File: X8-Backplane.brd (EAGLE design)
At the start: 101.6 x 101.6 mm, 4 parts

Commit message: Fleshing out the idea for the backplane
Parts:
- moved U$18 94.3 mm to (26.2, 82.3), turned to 270 degrees
- moved U$2 31.6 mm to (54.4, 31.8)
- moved U$1 22.7 mm to (89.2, 39.6)
- moved U$17 9.80 mm to (69.6, 39.9)
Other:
- outline, holes or cut-outs redrawn
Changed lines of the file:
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@@
 <setting verticaltext="up"/>
 </settings>
-<grid distance="0.05" unitdist="inch" unit="inch" style="lines" multiple="1" display="no" altdistance="0.025" altunitdist="inch" altunit="inch"/>
+<grid distance="0.01" unitdist="inch" unit="inch" style="lines" multiple="1" display="no" altdistance="0.025" altunitdist="inch" altunit="inch"/>
 <layers>
 <layer number="1" name="Top" color="4" fill="1" visible="yes" active="yes"/>
@@
 <layer number="42" name="bRestrict" color="1" fill="10" visible="no" active="yes"/>
 <layer number="43" name="vRestrict" color="2" fill="10" visible="no" active="yes"/>
-<layer number="44" name="Drills" color="7" fill="1" visible="yes" active="yes"/>
+<layer number="44" name="Drills" color="7" fill="1" visible="no" active="yes"/>
 <layer number="45" name="Holes" color="7" fill="1" visible="yes" active="yes"/>
-<layer number="46" name="Milling" color="3" fill="1" visible="yes" active="yes"/>
-<layer number="47" name="Measures" color="7" fill="1" visible="yes" active="yes"/>
-<layer number="48" name="Document" color="7" fill="1" visible="yes" active="yes"/>
+<layer number="46" name="Milling" color="3" fill="1" visible="no" active="yes"/>
+<layer number="47" name="Measures" color="7" fill="1" visible="no" active="yes"/>
+<layer number="48" name="Document" color="7" fill="1" visible="no" active="yes"/>
 <layer number="49" name="Reference" color="7" fill="1" visible="no" active="yes"/>
 <layer number="50" name="dxf" color="7" fill="1" visible="no" active="no"/>
-<layer number="51" name="tDocu" color="7" fill="1" visible="no" active="yes"/>
-<layer number="52" name="bDocu" color="7" fill="1" visible="no" active="yes"/>
+<layer number="51" name="tDocu" color="7" fill="1" visible="yes" active="yes"/>
+<layer number="52" name="bDocu" color="7" fill="1" visible="yes" active="yes"/>
 <layer number="53" name="tGND_GNDA" color="7" fill="1" visible="no" active="no"/>
 <layer number="54" name="bGND_GNDA" color="7" fill="1" visible="no" active="no"/>
@@
 <wire x1="100" y1="0" x2="100" y2="80" width="0" layer="20"/>
 <wire x1="100" y1="80" x2="0" y2="80" width="0" layer="20"/>
-<wire x1="0" y1="80" x2="0" y2="0" width="0" layer="20"/>
-<circle x="50.8" y="38.1" radius="50.8" width="0.4064" layer="20"/>
+<wire x1="0" y1="80" x2="0" y2="59.69" width="0" layer="20"/>
+<wire x1="0" y1="17.78" x2="0" y2="0" width="0" layer="20"/>
+<wire x1="0" y1="59.69" x2="0" y2="17.78" width="0.4064" layer="20"/>
+<wire x1="29.21" y1="-12.7" x2="72.39" y2="-12.7" width="0.4064" layer="20"/>
+<wire x1="101.6" y1="17.78" x2="101.6" y2="59.69" width="0.4064" layer="20"/>
+<wire x1="72.39" y1="88.9" x2="29.21" y2="88.9" width="0.4064" layer="20"/>
+<wire x1="0" y1="59.69" x2="14.732" y2="74.422" width="0.4064" layer="20"/>
+<wire x1="14.732" y1="74.422" x2="29.21" y2="88.9" width="0.4064" layer="20"/>
+<wire x1="29.21" y1="-12.7" x2="0" y2="17.78" width="0.4064" layer="20"/>
+<wire x1="101.6" y1="59.69" x2="72.39" y2="88.9" width="0.4064" layer="20"/>
+<wire x1="101.6" y1="17.78" x2="72.39" y2="-12.7" width="0.4064" layer="20"/>
+<hole x="21.59" y="67.818" drill="3.2"/>
+<hole x="80.01" y="66.802" drill="3.2"/>
+<hole x="21.59" y="9.398" drill="3.2"/>
+<hole x="80.01" y="9.398" drill="3.2"/>
+<wire x1="14.986" y1="74.422" x2="14.732" y2="74.422" width="0.4064" layer="20"/>
 </plain>
 <attributes>
@@
 </autorouter>
 <elements>
-<element name="U$1" library="HSEC8-1xx-01-XX-DV-A" package="HSEC8-140-01-XX-DV-A" value="HSEC8-140-01-XX-DV-A" x="67.31" y="45.72" rot="R90"/>
-<element name="U$17" library="HSEC8-1xx-01-XX-DV-A" package="HSEC8-140-01-XX-DV-A" value="HSEC8-140-01-XX-DV-A" x="77.47" y="45.72" rot="R90"/>
-<element name="U$2" library="HSEC8-1xx-01-XX-DV-A" package="HSEC8-160-01-XX-DV-A" value="HSEC8-160-01-XX-DV-A" x="25.4" y="44.45" rot="R90"/>
-<element name="U$18" library="Other" package="ETH_SWITCH" value="" x="58.42" y="-6.35" rot="R90"/>
+<element name="U$1" library="HSEC8-1xx-01-XX-DV-A" package="HSEC8-140-01-XX-DV-A" value="HSEC8-140-01-XX-DV-A" x="89.154" y="39.624" rot="R90"/>
+<element name="U$17" library="HSEC8-1xx-01-XX-DV-A" package="HSEC8-140-01-XX-DV-A" value="HSEC8-140-01-XX-DV-A" x="69.596" y="39.878" rot="R90"/>
+<element name="U$18" library="Other" package="ETH_SWITCH" value="" x="26.162" y="82.296" rot="R270"/>
+<element name="U$2" library="HSEC8-1xx-01-XX-DV-A" package="HSEC8-160-01-XX-DV-A" value="HSEC8-160-01-XX-DV-A" x="54.356" y="31.75" rot="R90"/>
 </elements>
 <signals>

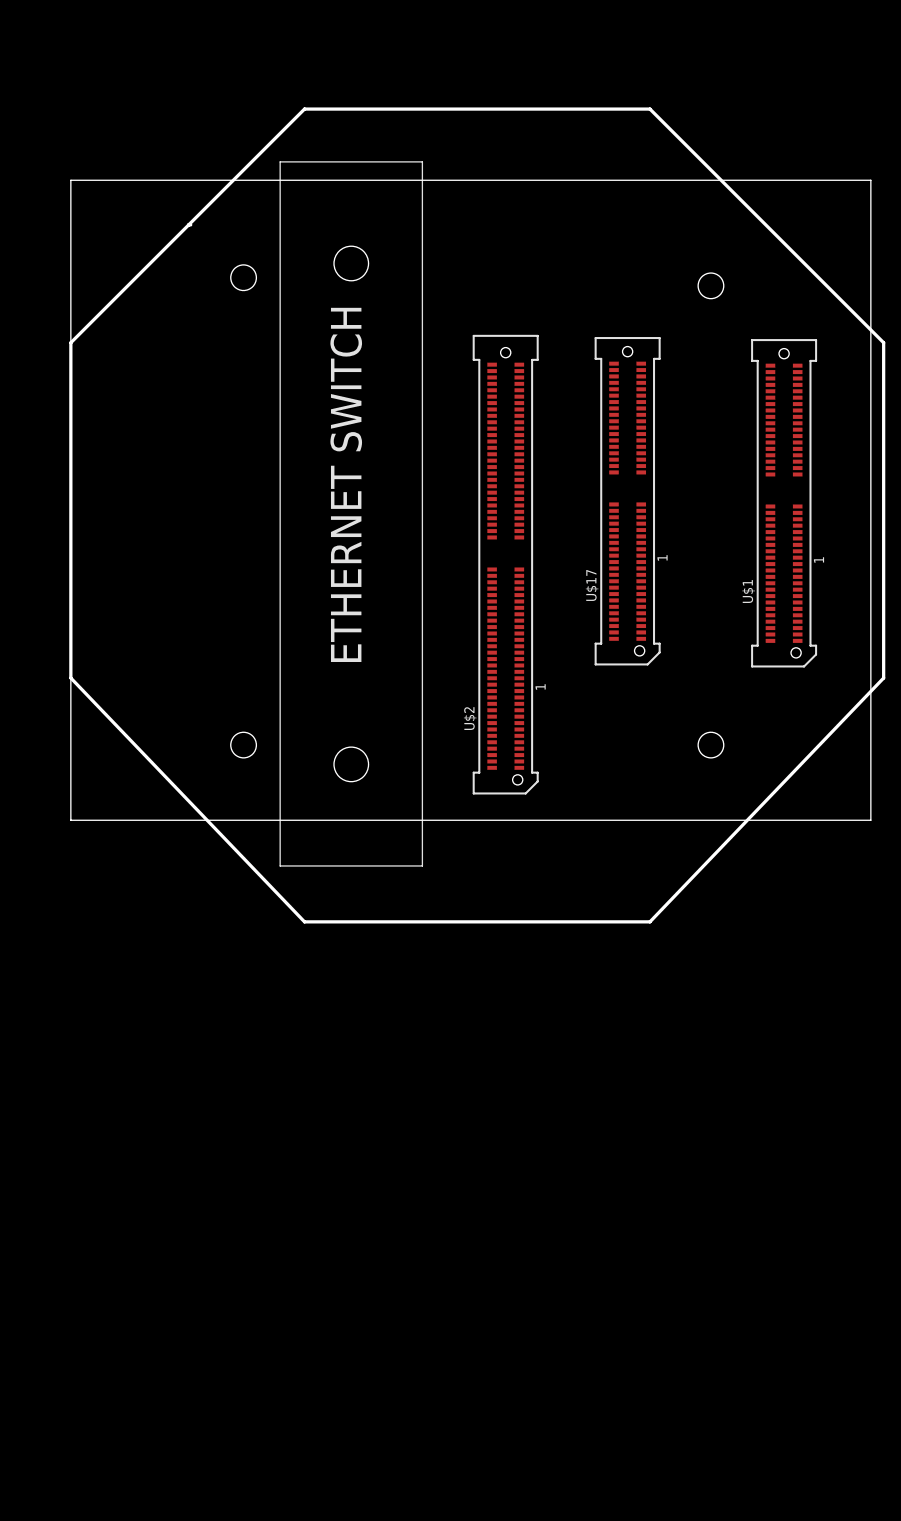
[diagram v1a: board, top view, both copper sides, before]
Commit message: Added more connections to the backplane
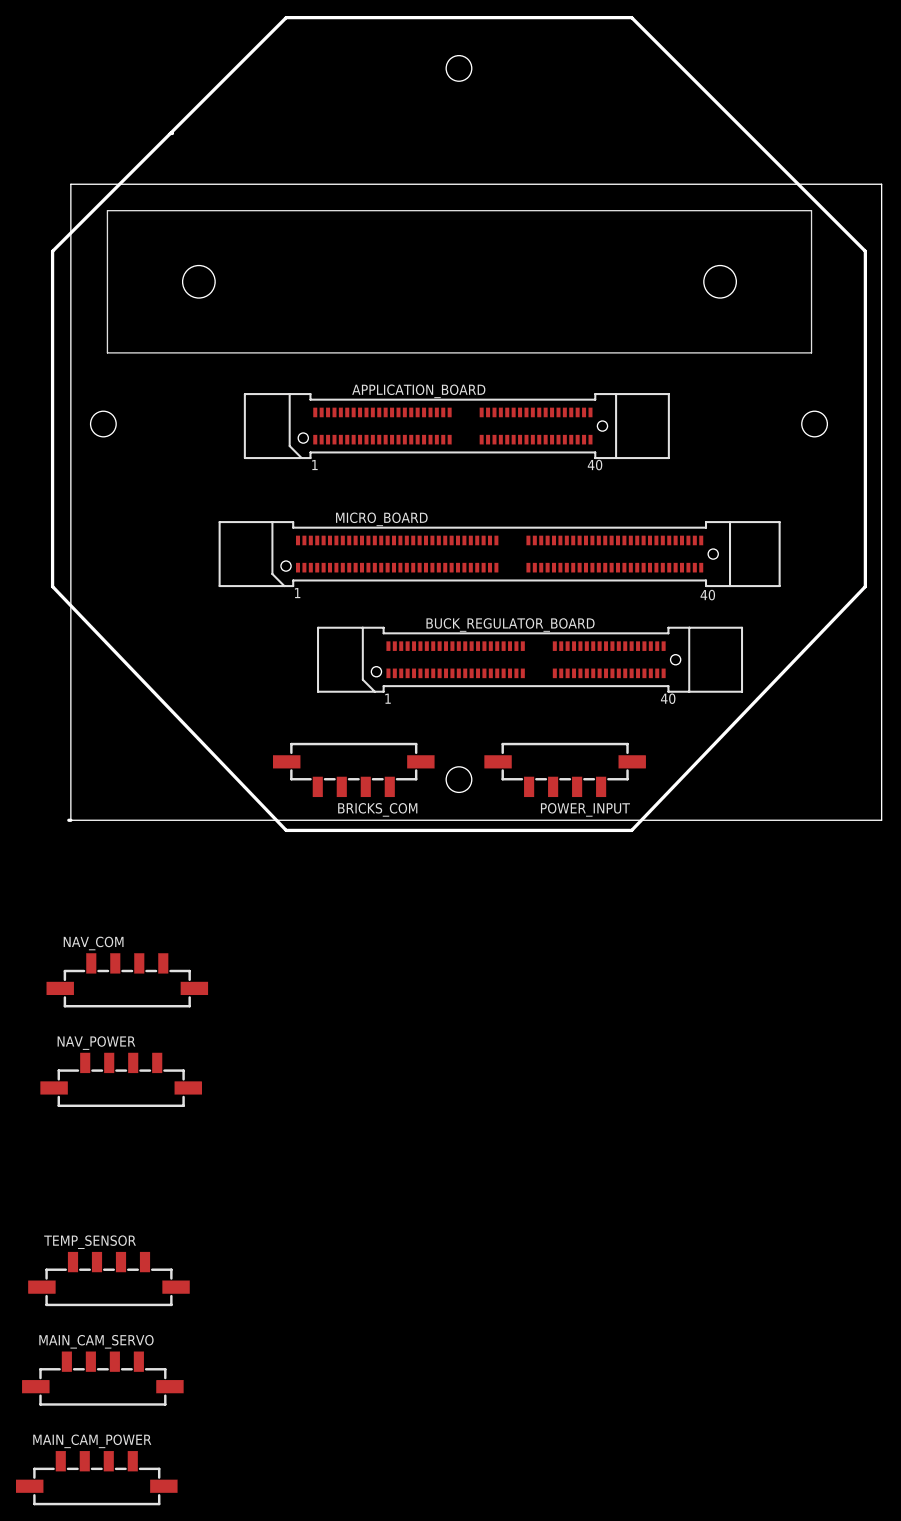
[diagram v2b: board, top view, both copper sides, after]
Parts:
- removed U$1, U$17: HSEC8-140-01-XX-DV-A, HSEC8-1xx-01-XX-DV-A:HSEC8-140-01-XX-DV-A
- removed U$2: HSEC8-160-01-XX-DV-A, HSEC8-1xx-01-XX-DV-A:HSEC8-160-01-XX-DV-A
- added APPLICATION_BOARD, BUCK_REGULATOR_BOARD: HSEC8-140-01-XX-DV-A, HSEC8-1xx-01-XX-DV-A:HSEC8-140-01-XX-DV-A
- added BRICKS_COM, MAIN_CAM_POWER, MAIN_CAM_SERVO, NAV_COM, NAV_POWER, POWER_INPUT, TEMP_SENSOR: MICRO-FIT-4-SMD-PART, Connectors:MICRO-FIT-4-SMD
- added MICRO_BOARD: HSEC8-160-01-XX-DV-A, HSEC8-1xx-01-XX-DV-A:HSEC8-160-01-XX-DV-A
- moved U$18 32.2 mm to (4.57, 58.4), turned to 0 degrees
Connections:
- new net +12V: BUCK_REGULATOR_BOARD.31, BUCK_REGULATOR_BOARD.32, BUCK_REGULATOR_BOARD.33, BUCK_REGULATOR_BOARD.34, BUCK_REGULATOR_BOARD.35, BUCK_REGULATOR_BOARD.36, BUCK_REGULATOR_BOARD.37, BUCK_REGULATOR_BOARD.38, BUCK_REGULATOR_BOARD.39, BUCK_REGULATOR_BOARD.40, BUCK_REGULATOR_BOARD.41, BUCK_REGULATOR_BOARD.42, BUCK_REGULATOR_BOARD.43, BUCK_REGULATOR_BOARD.44, BUCK_REGULATOR_BOARD.45, BUCK_REGULATOR_BOARD.46, BUCK_REGULATOR_BOARD.47, BUCK_REGULATOR_BOARD.48, BUCK_REGULATOR_BOARD.49, BUCK_REGULATOR_BOARD.50, BUCK_REGULATOR_BOARD.51, BUCK_REGULATOR_BOARD.52, MAIN_CAM_POWER.C4, NAV_POWER.C4, POWER_INPUT.C3, POWER_INPUT.C4
- new net +3V3: TEMP_SENSOR.C3
- new net +5V: BUCK_REGULATOR_BOARD.10, BUCK_REGULATOR_BOARD.11, BUCK_REGULATOR_BOARD.12, BUCK_REGULATOR_BOARD.13, BUCK_REGULATOR_BOARD.14, BUCK_REGULATOR_BOARD.15, BUCK_REGULATOR_BOARD.16, BUCK_REGULATOR_BOARD.17, BUCK_REGULATOR_BOARD.18, BUCK_REGULATOR_BOARD.19, BUCK_REGULATOR_BOARD.20, BUCK_REGULATOR_BOARD.21, BUCK_REGULATOR_BOARD.22, BUCK_REGULATOR_BOARD.23, BUCK_REGULATOR_BOARD.24, BUCK_REGULATOR_BOARD.25, BUCK_REGULATOR_BOARD.26, BUCK_REGULATOR_BOARD.5, BUCK_REGULATOR_BOARD.6, BUCK_REGULATOR_BOARD.7, BUCK_REGULATOR_BOARD.8, BUCK_REGULATOR_BOARD.9, MAIN_CAM_SERVO.C3, NAV_POWER.C3
- new net BUCK_SCL: BUCK_REGULATOR_BOARD.1, BUCK_REGULATOR_BOARD.2
- new net BUCK_SDA: BUCK_REGULATOR_BOARD.3, BUCK_REGULATOR_BOARD.4
- new net CANH: BRICKS_COM.C4
- new net CANL: BRICKS_COM.C3
- new net GND: BUCK_REGULATOR_BOARD.55, BUCK_REGULATOR_BOARD.56, BUCK_REGULATOR_BOARD.57, BUCK_REGULATOR_BOARD.58, BUCK_REGULATOR_BOARD.59, BUCK_REGULATOR_BOARD.60, BUCK_REGULATOR_BOARD.61, BUCK_REGULATOR_BOARD.62, BUCK_REGULATOR_BOARD.63, BUCK_REGULATOR_BOARD.64, BUCK_REGULATOR_BOARD.65, BUCK_REGULATOR_BOARD.66, BUCK_REGULATOR_BOARD.67, BUCK_REGULATOR_BOARD.68, BUCK_REGULATOR_BOARD.69, BUCK_REGULATOR_BOARD.70, BUCK_REGULATOR_BOARD.71, BUCK_REGULATOR_BOARD.72, BUCK_REGULATOR_BOARD.73, BUCK_REGULATOR_BOARD.74, BUCK_REGULATOR_BOARD.75, BUCK_REGULATOR_BOARD.76, BUCK_REGULATOR_BOARD.77, BUCK_REGULATOR_BOARD.78, BUCK_REGULATOR_BOARD.79, BUCK_REGULATOR_BOARD.80, MAIN_CAM_POWER.C1, MAIN_CAM_POWER.C2, MAIN_CAM_SERVO.C2, NAV_POWER.C1, NAV_POWER.C2, POWER_INPUT.C1, POWER_INPUT.C2, TEMP_SENSOR.C2
- new net LED_PWM: MAIN_CAM_POWER.C3
- new net MAIN_SERVO: MAIN_CAM_SERVO.C4
- new net N$3: BRICKS_COM.C2
- new net N$5: BRICKS_COM.C1
- new net N$7: TEMP_SENSOR.C1
- new net SCL: NAV_COM.C4
- new net SDA: NAV_COM.C3
- new net SONAR_DAC: NAV_COM.C1
- new net SONAR_PWM: NAV_COM.C2
- new net TEMP_DATA: TEMP_SENSOR.C4
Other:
- board size 101.6 x 101.6 mm -> 103.6 x 101.6 mm

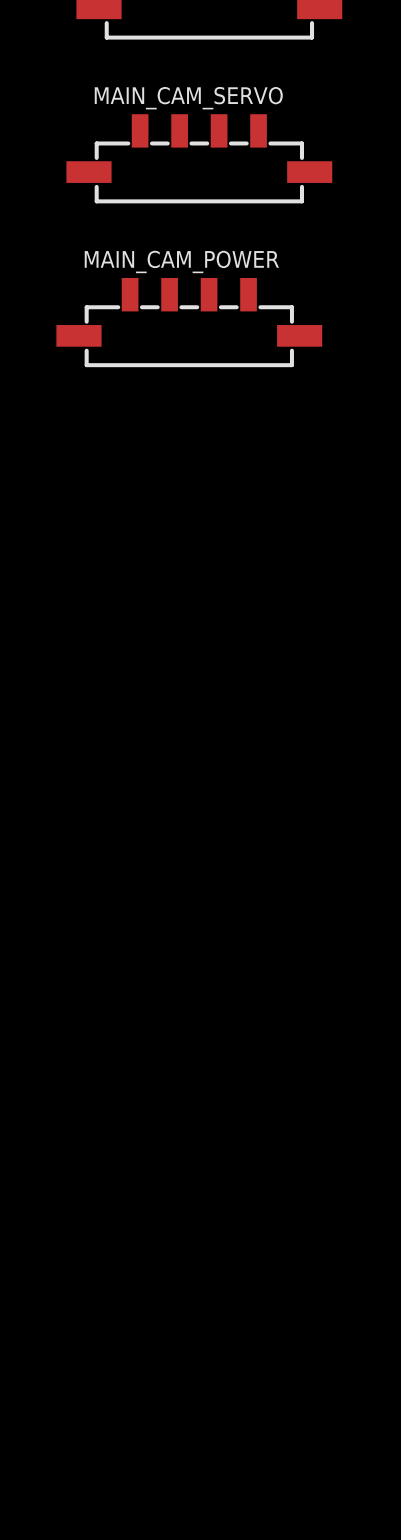
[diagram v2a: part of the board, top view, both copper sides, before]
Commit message: Added more connectors to the backplane schematic
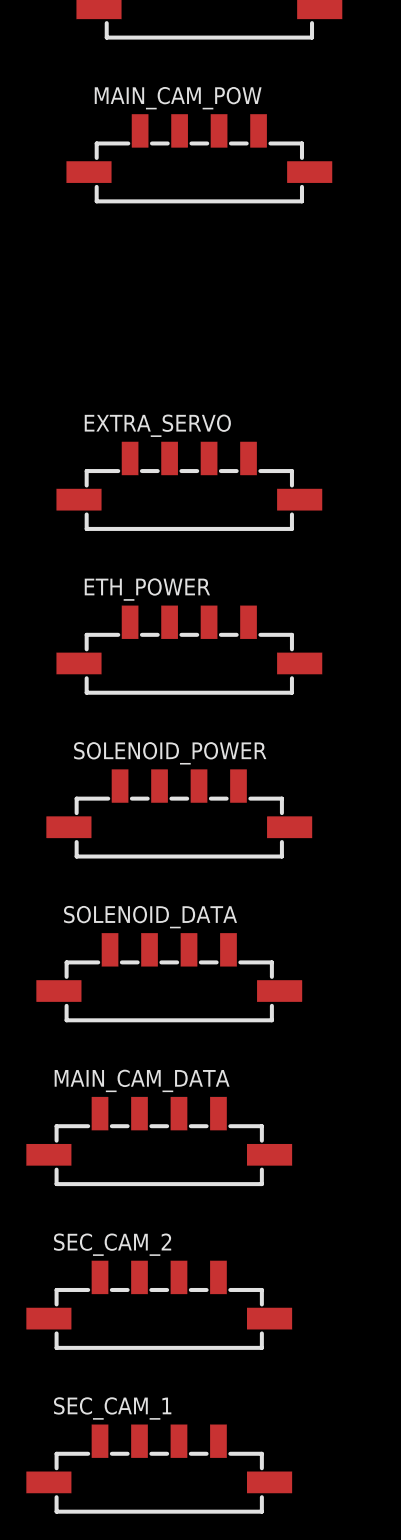
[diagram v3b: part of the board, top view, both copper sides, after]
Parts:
- removed MAIN_CAM_POWER: MICRO-FIT-4-SMD-PART, Connectors:MICRO-FIT-4-SMD
- added ETH_POWER, EXTRA_SERVO, MAIN_CAM_DATA, SEC_CAM_1, SEC_CAM_2, SOLENOID_DATA, SOLENOID_POWER: MICRO-FIT-4-SMD-PART, Connectors:MICRO-FIT-4-SMD
- renumbered MAIN_CAM_SERVO to MAIN_CAM_POW
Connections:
- new net CLK: SOLENOID_DATA.C3
- new net DATA: SOLENOID_DATA.C1
- new net ENABLE: SOLENOID_DATA.C2
- new net SECOND_SERVO: EXTRA_SERVO.C4
- net +12V: now also MAIN_CAM_POW.C4, SEC_CAM_1.C3, SEC_CAM_1.C4, SEC_CAM_2.C3, SEC_CAM_2.C4, SOLENOID_POWER.C3, SOLENOID_POWER.C4; no longer MAIN_CAM_POWER.C4
- net +5V: now also ETH_POWER.C3, ETH_POWER.C4, EXTRA_SERVO.C3, MAIN_CAM_POW.C2, SOLENOID_DATA.C4
- net GND: now also ETH_POWER.C1, ETH_POWER.C2, EXTRA_SERVO.C2, MAIN_CAM_DATA.C1, MAIN_CAM_DATA.C2, MAIN_CAM_POW.C1, SEC_CAM_1.C1, SEC_CAM_1.C2, SEC_CAM_2.C1, SEC_CAM_2.C2, SOLENOID_POWER.C1, SOLENOID_POWER.C2; no longer MAIN_CAM_POW.C2, MAIN_CAM_POWER.C1, MAIN_CAM_POWER.C2
- net LED_PWM: now also MAIN_CAM_DATA.C3; no longer MAIN_CAM_POWER.C3
- net MAIN_SERVO: now also MAIN_CAM_DATA.C4; no longer MAIN_CAM_POW.C4

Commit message: First placement of parts
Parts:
- removed MAIN_CAM_POW: MICRO-FIT-4-SMD-PART, Connectors:MICRO-FIT-4-SMD
- added MA5N_CAM_POW: MICRO-FIT-4-SMD-PART, Connectors:MICRO-FIT-4-SMD
- moved SEC_CAM_1 275.0 mm to (72.4, 91.4), flipped to the bottom
- moved SEC_CAM_2 252.3 mm to (72.4, 80.0), flipped to the bottom
- moved ETH_POWER 195.8 mm to (44.5, 80.0), flipped to the bottom
- moved SOLENOID_POWER 195.7 mm to (72.4, 57.1), flipped to the bottom
- moved EXTRA_SERVO 194.8 mm to (44.5, 91.4), flipped to the bottom
- moved MAIN_CAM_DATA 165.0 mm to (47.0, 8.89), flipped to the bottom
- moved SOLENOID_DATA 147.8 mm to (22.4, 10.7), flipped to the bottom, turned to 45 degrees
- moved TEMP_SENSOR 143.2 mm to (88.1, 49.3), flipped to the bottom, turned to 270 degrees
- moved NAV_POWER 113.6 mm to (44.5, 68.6), flipped to the bottom
- moved NAV_COM 102.8 mm to (88.6, 24.6), flipped to the bottom, turned to 315 degrees
- moved POWER_INPUT 60.5 mm to (72.4, 68.6), flipped to the bottom, turned to 0 degrees
- moved BUCK_REGULATOR_BOARD 30.5 mm to (46.5, 48.8)
- moved APPLICATION_BOARD 27.2 mm to (46.0, 22.1)
- moved BRICKS_COM 24.6 mm to (70.1, 8.89), flipped to the bottom, turned to 0 degrees
- moved MICRO_BOARD 7.41 mm to (46.7, 36.1)
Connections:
- net +12V: now also MA5N_CAM_POW.C1, NAV_POWER.C1; no longer MAIN_CAM_POW.C4, NAV_POWER.C4
- net +5V: now also ETH_POWER.C1, ETH_POWER.C2, EXTRA_SERVO.C2, MA5N_CAM_POW.C2, MA5N_CAM_POW.C3, NAV_POWER.C2, SOLENOID_DATA.C1; no longer ETH_POWER.C3, ETH_POWER.C4, EXTRA_SERVO.C3, MAIN_CAM_POW.C2, MAIN_CAM_POW.C3, NAV_POWER.C3, SOLENOID_DATA.C4
- net DATA: now also SOLENOID_DATA.C4; no longer SOLENOID_DATA.C1
- net GND: now also ETH_POWER.C3, ETH_POWER.C4, EXTRA_SERVO.C3, MA5N_CAM_POW.C4, NAV_POWER.C3, NAV_POWER.C4; no longer ETH_POWER.C1, ETH_POWER.C2, EXTRA_SERVO.C2, MAIN_CAM_POW.C1, NAV_POWER.C1, NAV_POWER.C2
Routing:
- added copper zone on layer 1, net +12V
- added copper zone on layer 16, net +12V
- added copper zone on layer 1, net +5V
- added copper zone on layer 16, net +5V
- added copper zone on layer 1, net GND
- added copper zone on layer 16, net GND
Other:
- board size 103.6 x 101.6 mm -> 101.9 x 101.6 mm
